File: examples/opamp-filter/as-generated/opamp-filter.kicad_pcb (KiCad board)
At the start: 2 copper layers, 58 x 42 mm, 22 parts, among them J1 IN, J2 5V, J3 OUT, U1 MCP6001R, U2 MCP6001R

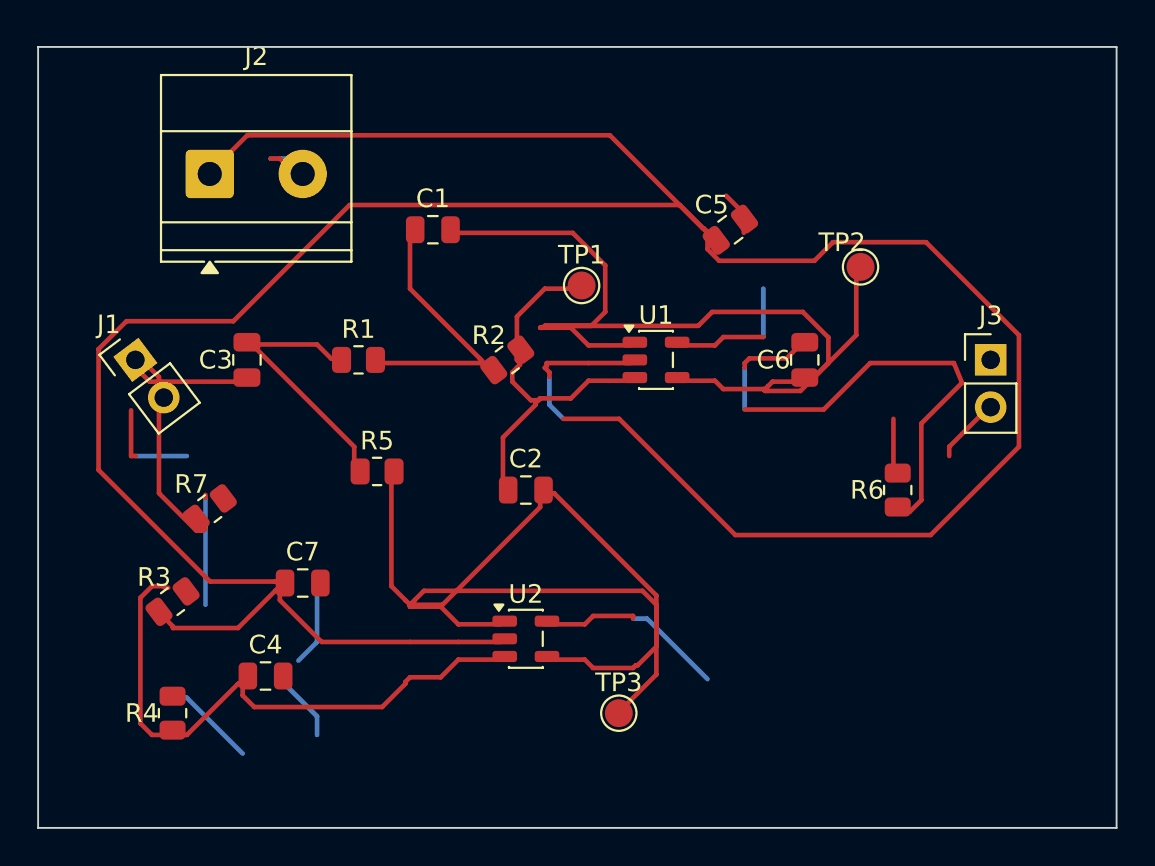
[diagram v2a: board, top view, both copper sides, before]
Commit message: Give a turned part's designator somewhere to go
A designator prints horizontally whatever the footprint's rotation, so
on a part turned 90 degrees the string reaches along the axis the
footprint's own frame calls the other one - and a two-terminal chip part
is narrower than its own three-character name. Every spot inside the
footprint touched a pad, and the search gave up and left it there.

It now looks along both local axes, at increasing distance, starting
from half the string plus half the part. Near still beats far.

The fold-back pass also stops refusing to unfold a run that walks back
past where it set out from. That refusal was there because deleting the
point moves the corner before it; usually that corner is the other half
of the same fold and both go. Now it checks: if what is left is 90
degrees or wider, unfold; if not, the run keeps its spur rather than
trade it for a worse bend.
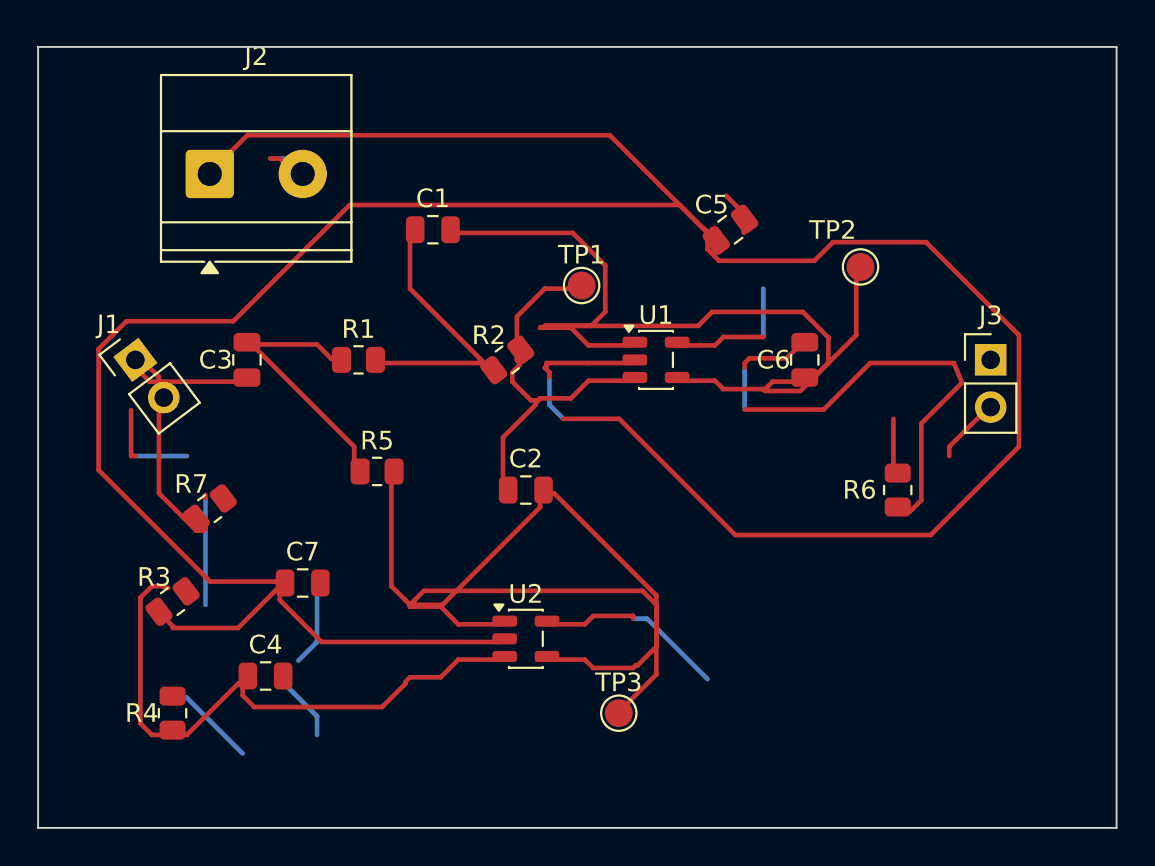
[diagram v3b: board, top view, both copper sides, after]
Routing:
- net /IN_DC: track 15.4 -> 14.8 mm
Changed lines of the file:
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@@
     (tags "resistor")
     (property "Reference" "R6"
-      (at 0 -1.65 0)
+      (at 0.0 -2.05 0)
       (layer "F.SilkS")
       (effects
@@
     )
     (property "Datasheet" "https://www.yageo.com/upload/media/product/productsearch/datasheet/rchip/PYu-RC_Group_51_RoHS_L_12.pdf"
-      (at 0 -1.65 0)
+      (at 0.0 -2.05 0)
       (layer "F.Fab")
       (hide yes)
@@
     (tags "test point SMD pad")
     (property "Reference" "TP2"
-      (at 0 -1.648 0)
+      (at 0.0 -2.475 0)
       (layer "F.SilkS")
       (effects
@@
 	(segment (start 115.75 76.75) (end 115.0 76.0) (width 0.25) (layer "F.Cu") (net 5))
 	(segment (start 115.0 76.0) (end 111.25 76.0) (width 0.25) (layer "F.Cu") (net 5))
-	(segment (start 111.25 76.0) (end 111.2 76.05) (width 0.25) (layer "F.Cu") (net 5))
-	(segment (start 111.2 76.05) (end 111.0 76.05) (width 0.25) (layer "F.Cu") (net 5))
-	(segment (start 111.0 76.05) (end 111.2 76.05) (width 0.25) (layer "F.Cu") (net 5))
-	(segment (start 111.2 76.05) (end 111.25 76.0) (width 0.25) (layer "F.Cu") (net 5))
 	(segment (start 111.25 76.0) (end 111.5 76.0) (width 0.25) (layer "F.Cu") (net 5))
 	(segment (start 111.5 76.0) (end 117.0 81.5) (width 0.25) (layer "F.Cu") (net 5))
